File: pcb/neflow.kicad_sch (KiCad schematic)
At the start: 54 parts, among them J1 Conn_01x02_Socket, J2 Conn_01x02_Socket, J3 SSR0, J4 SSR1, J5 Conn_01x02_Socket, J7 FAN1, J8 FAN0, Q1 IRLML2502, Q2 IRLML2502, Q3 IRLML2502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

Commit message: Add silicone_btn and pcb
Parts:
- SW1, SW2, SW3, SW4: footprint (none) -> silicone_btn:BUTTON_SILICON
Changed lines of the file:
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@@
       (effects (font (size 1.27 1.27)))
     )
-    (property "Footprint" "" (at 142.24 86.36 0)
+    (property "Footprint" "silicone_btn:BUTTON_SILICON" (at 142.24 86.36 0)
       (effects (font (size 1.27 1.27)) hide)
     )
@@
       (effects (font (size 1.27 1.27)))
     )
-    (property "Footprint" "" (at 170.18 86.36 0)
+    (property "Footprint" "silicone_btn:BUTTON_SILICON" (at 170.18 86.36 0)
       (effects (font (size 1.27 1.27)) hide)
     )
@@
       (effects (font (size 1.27 1.27)))
     )
-    (property "Footprint" "" (at 142.24 104.14 0)
+    (property "Footprint" "silicone_btn:BUTTON_SILICON" (at 142.24 104.14 0)
       (effects (font (size 1.27 1.27)) hide)
     )
@@
       (effects (font (size 1.27 1.27)))
     )
-    (property "Footprint" "" (at 170.18 104.14 0)
-      (effects (font (size 1.27 1.27)) hide)
-    )
+    (property "Footprint" "silicone_btn:BUTTON_SILICON" (at 170.18 104.14 0)
+      (effects (font (size 1.27 1.27)) hide)
+    )

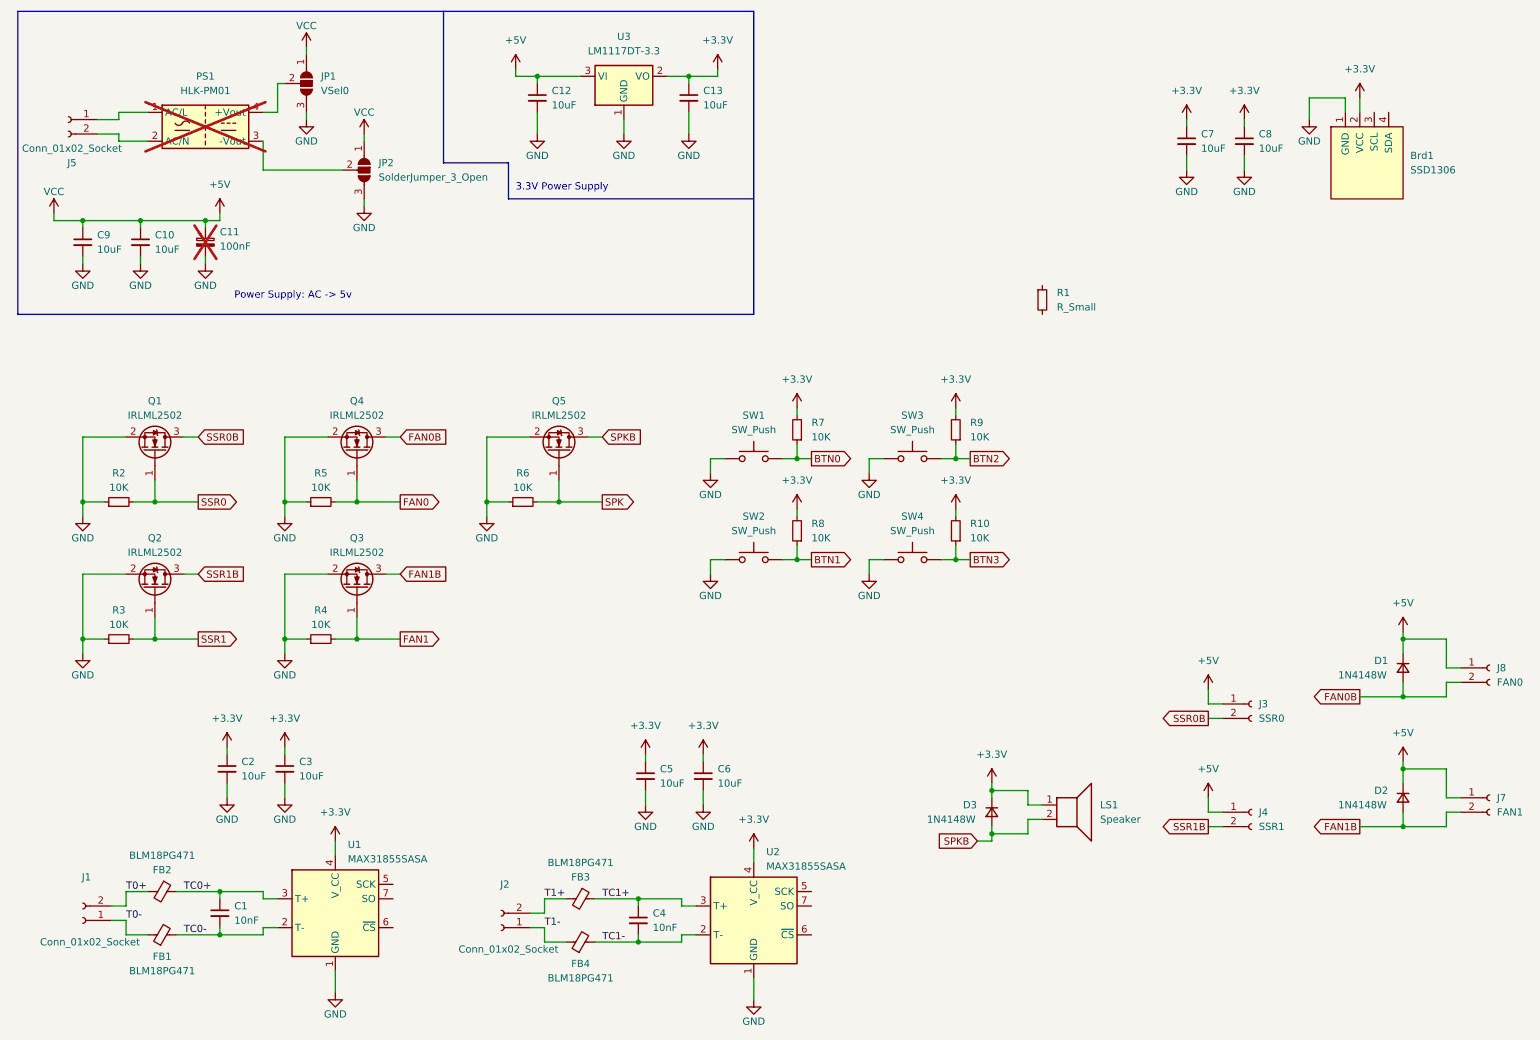
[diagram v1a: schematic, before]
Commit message: Adding almost finished schematic
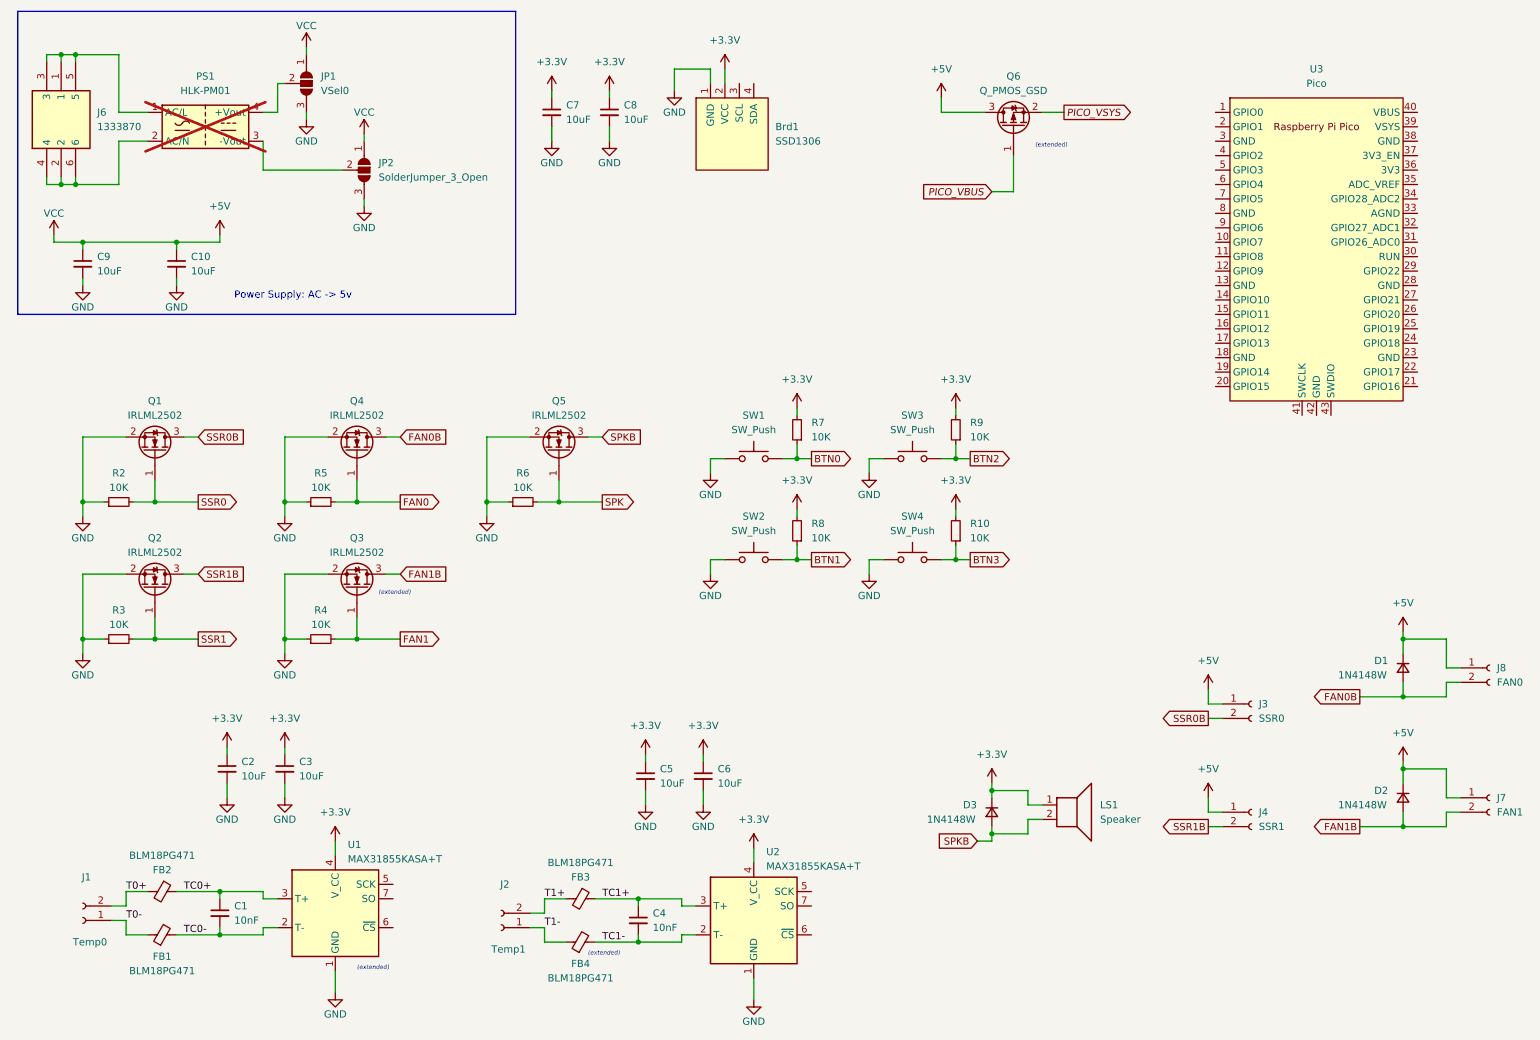
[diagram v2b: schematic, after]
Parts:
- removed C11: 100nF, symbol Device:C_Polarized_Small
- removed C12, C13: 10uF, symbol Device:C_Small
- removed J5: Conn_01x02_Socket, symbol Connector:Conn_01x02_Socket
- removed R1: R_Small, symbol Device:R_Small
- removed U3: LM1117DT-3.3, Package_TO_SOT_SMD:TO-252-3_TabPin2, symbol Regulator_Linear:LM1117DT-3.3
- added J6: 1333870, Unsharable:1333870, symbol 1333870:1333870
- added Q6: Q_PMOS_GSD, Package_TO_SOT_SMD:SOT-23, symbol Device:Q_PMOS_GSD
- added U3: Pico, MCU_RaspberryPi_and_Boards:RPi_Pico_SMD_TH, symbol MCU_RaspberryPi_and_Boards:Pico
- C1, C10, C2, C3, C4, C5, C6, C7, C8, C9, R10, R2, R3, R4, R5, R6, R7, R8, R9: footprint (none) -> Resistor_SMD:R_0603_1608Metric
- D1, D2, D3: footprint (none) -> Diode_SMD:D_SOD-123
- J1: value Conn_01x02_Socket -> Temp0; footprint (none) -> Connector_JST:JST_XH_B2B-XH-AM_1x02_P2.50mm_Vertical
- J2: value Conn_01x02_Socket -> Temp1; footprint (none) -> Connector_JST:JST_XH_B2B-XH-AM_1x02_P2.50mm_Vertical
- J3, J4, J7, J8: footprint (none) -> Connector_JST:JST_XH_B2B-XH-AM_1x02_P2.50mm_Vertical
- JP1, JP2: footprint (none) -> Jumper:SolderJumper-3_P1.3mm_Open_Pad1.0x1.5mm
- PS1: now left out of the parts list
- U1, U2: value MAX31855SASA -> MAX31855KASA+T; LCSC (none) -> C52028
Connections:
- net +5V: now also Q6.3 (D)
- net at PS1.1 (AC/L): now also J6.1, J6.3, J6.5
- net at PS1.2 (AC/N): now also J6.2, J6.4, J6.6
- new net PICO_VBUS: Q6.1 (G)
- new net PICO_VSYS: Q6.2 (S)
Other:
- note added: "(extended)"
- note removed: "3.3V Power Supply"
- moved on the sheet: Brd1, C10, C7, C8, C9
